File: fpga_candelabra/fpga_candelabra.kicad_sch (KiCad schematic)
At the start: 0 parts

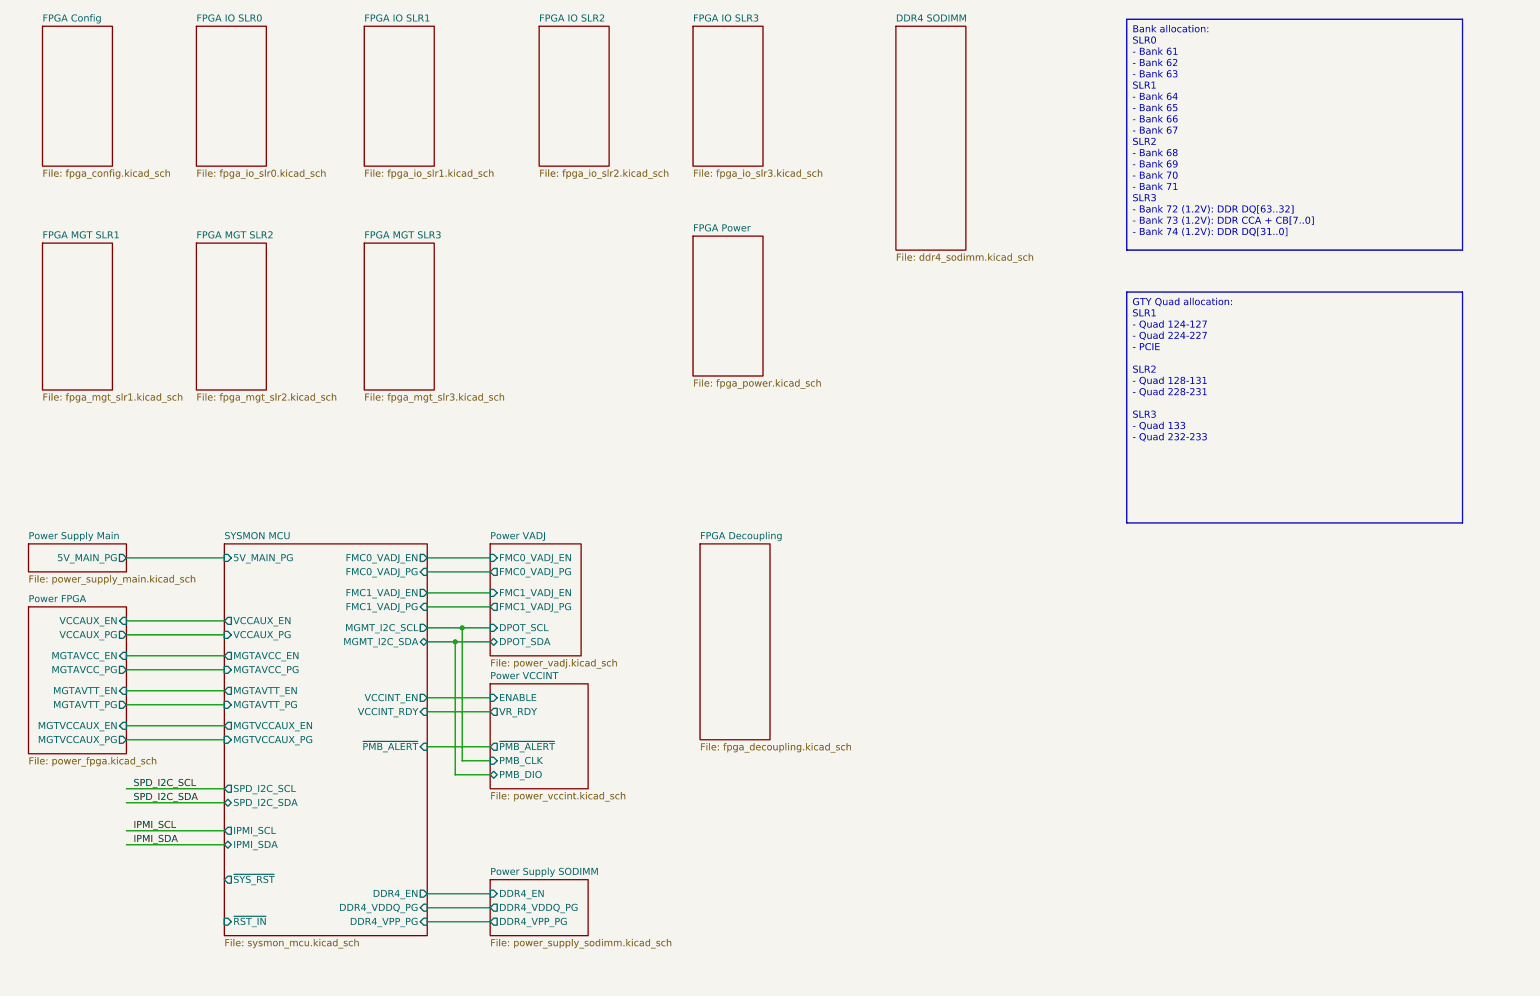
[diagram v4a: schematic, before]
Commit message: fpga_candelabra: use bus alias to connect ddr4
Signed-off-by: Yichuan Gao <gaoyichuan000@gmail.com>
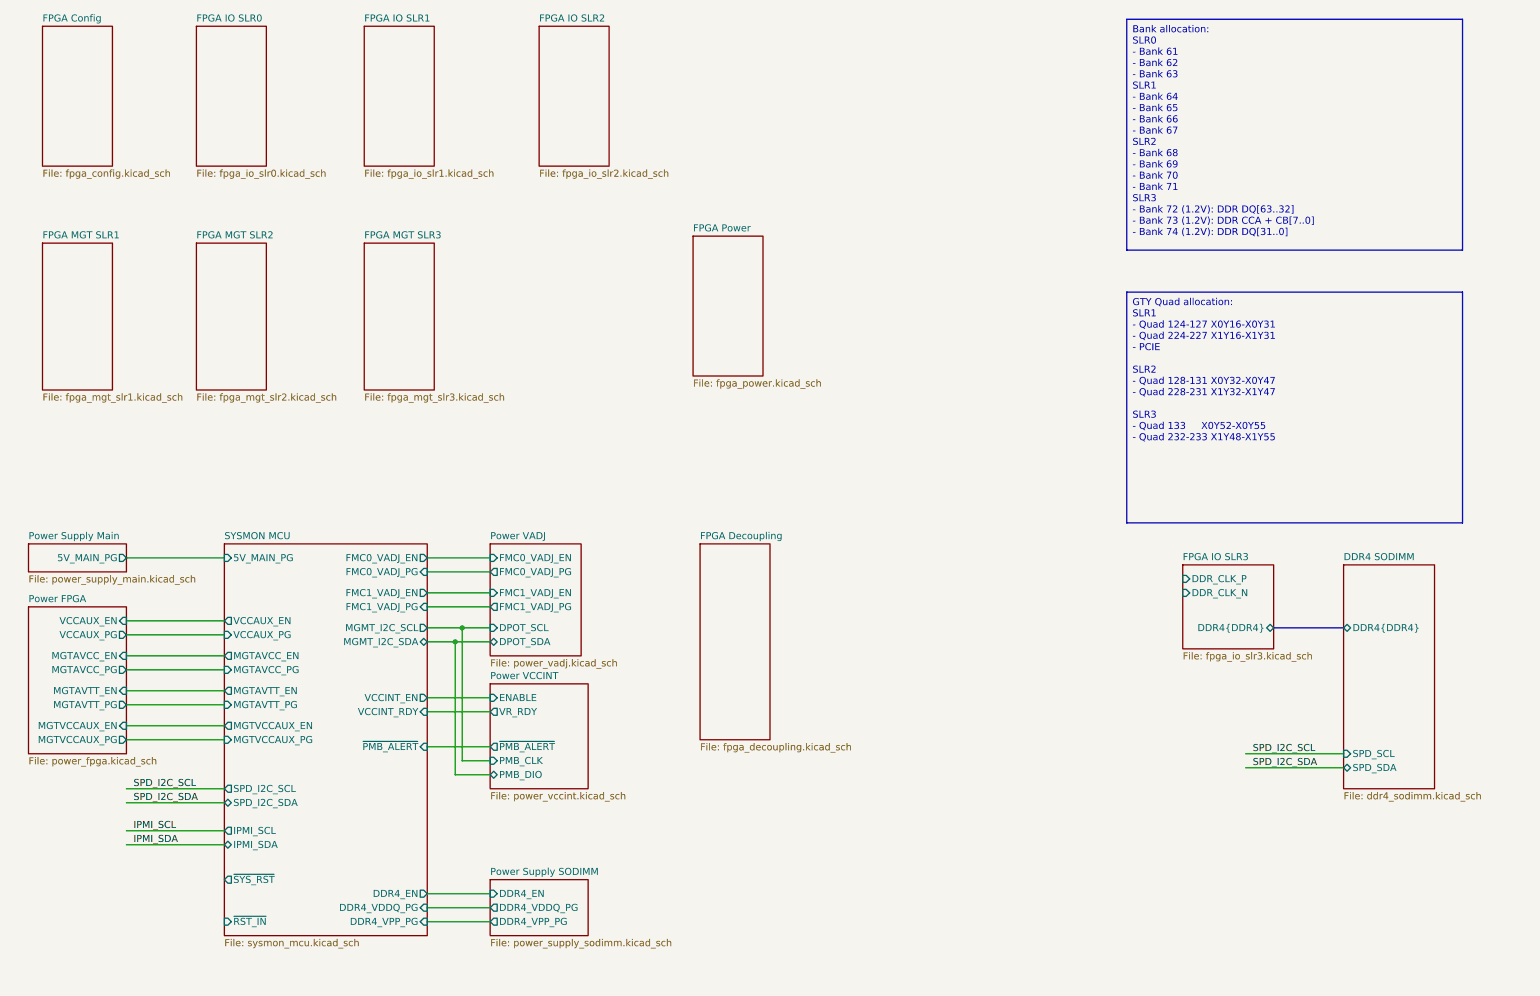
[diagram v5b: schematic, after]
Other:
- sheet DDR4 SODIMM ports: added DDR4{DDR4}, SPD_SCL, SPD_SDA; removed none
- sheet FPGA IO SLR3 ports: added DDR4{DDR4}, DDR_CLK_N, DDR_CLK_P; removed none
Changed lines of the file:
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@@
 	(generator_version "8.0")
 	(paper "A4")
+	(bus_alias "DDR4"
+		(members "A0" "A1" "A2" "A3" "A4" "A5" "A6" "A7" "A8" "A9" "A10" "A11"
+			"A12" "A13" "A14" "A15" "A16" "BA0" "BA1" "BG0" "BG1" "CK0+" "CK0-" "CKE0"
+			"CK1+" "CK1-" "CKE1" "CS0" "CS1" "CS2" "CS3" "ODT0" "ODT1" "~{ACT}" "PARITY"
+			"~{ALERT}" "~{RESET}" "DQS0+" "DQS1+" "DQS2+" "DQS3+" "DQS4+" "DQS5+"
+			"DQS6+" "DQS7+" "DQS8+" "DQS0-" "DQS1-" "DQS2-" "DQS3-" "DQS4-" "DQS5-"
+			"DQS6-" "DQS7-" "DQS8-" "DM0" "DM1" "DM2" "DM3" "DM4" "DM5" "DM6" "DM7"
+			"DM8" "DQ0" "DQ1" "DQ2" "DQ3" "DQ4" "DQ5" "DQ6" "DQ7" "DQ8" "DQ9" "DQ10"
+			"DQ11" "DQ12" "DQ13" "DQ14" "DQ15" "DQ16" "DQ17" "DQ18" "DQ19" "DQ20"
+			"DQ21" "DQ22" "DQ23" "DQ24" "DQ25" "DQ26" "DQ27" "DQ28" "DQ29" "DQ30"
+			"DQ31" "DQ32" "DQ33" "DQ34" "DQ35" "DQ36" "DQ37" "DQ38" "DQ39" "DQ40"
+			"DQ41" "DQ42" "DQ43" "DQ44" "DQ45" "DQ46" "DQ47" "DQ48" "DQ49" "DQ50"
+			"DQ51" "DQ52" "DQ53" "DQ54" "DQ55" "DQ56" "DQ57" "DQ58" "DQ59" "DQ60"
+			"DQ61" "DQ62" "DQ63" "CB0" "CB1" "CB2" "CB3" "CB4" "CB5" "CB6" "CB7"
+		)
+	)
 	(junction
 		(at 97.79 132.08)
@@
 		)
 	)
+	(bus
+		(pts
+			(xy 246.38 129.54) (xy 259.08 129.54)
+		)
+		(stroke
+			(width 0)
+			(type default)
+		)
+	)
 	(wire
 		(pts
@@
 	(wire
 		(pts
+			(xy 241.3 152.4) (xy 259.08 152.4)
+		)
+		(stroke
+			(width 0)
+			(type default)
+		)
+	)
+	(wire
+		(pts
 			(xy 38.1 128.27) (xy 55.88 128.27)
 		)
@@
 		(pts
 			(xy 99.06 153.67) (xy 104.14 153.67)
+		)
+		(stroke
+			(width 0)
+			(type default)
+		)
+	)
+	(wire
+		(pts
+			(xy 241.3 154.94) (xy 259.08 154.94)
 		)
 		(stroke
@@
 		)
 	)
-	(text_box "GTY Quad allocation:\nSLR1\n  - Quad 124-127\n  - Quad 224-227\n    - PCIE\n\nSLR2\n  - Quad 128-131\n  - Quad 228-231\n\nSLR3\n  - Quad 133\n  - Quad 232-233"
+	(text_box "GTY Quad allocation:\nSLR1\n  - Quad 124-127 X0Y16-X0Y31\n  - Quad 224-227 X1Y16-X1Y31\n    - PCIE\n\nSLR2\n  - Quad 128-131 X0Y32-X0Y47\n  - Quad 228-231 X1Y32-X1Y47\n\nSLR3\n  - Quad 133     X0Y52-X0Y55\n  - Quad 232-233 X1Y48-X1Y55"
 		(exclude_from_sim no)
 		(at 219.71 68.58 0)
@@
 		)
 	)
+	(label "SPD_I2C_SDA"
+		(at 242.57 154.94 0)
+		(fields_autoplaced yes)
+		(effects
+			(font
+				(size 1.27 1.27)
+			)
+			(justify left bottom)
+		)
+	)
 	(label "IPMI_SDA"
 		(at 39.37 168.91 0)
+		(fields_autoplaced yes)
+		(effects
+			(font
+				(size 1.27 1.27)
+			)
+			(justify left bottom)
+		)
+	)
+	(label "SPD_I2C_SCL"
+		(at 242.57 152.4 0)
 		(fields_autoplaced yes)
 		(effects
@@
 	)
 	(sheet
-		(at 140.97 20.32)
-		(size 12.7 25.4)
+		(at 229.87 118.11)
+		(size 16.51 15.24)
 		(fields_autoplaced yes)
 		(stroke
@@
 		)
 		(property "Sheetname" "FPGA IO SLR3"
-			(at 140.97 19.6084 0)
+			(at 229.87 117.3984 0)
 			(effects
 				(font
@@
 		)
 		(property "Sheetfile" "fpga_io_slr3.kicad_sch"
-			(at 140.97 46.3046 0)
+			(at 229.87 133.9346 0)
 			(effects
 				(font
@@
 				)
 				(justify left top)
+			)
+		)
+		(pin "DDR_CLK_N" input
+			(at 229.87 123.19 180)
+			(effects
+				(font
+					(size 1.27 1.27)
+				)
+				(justify left)
+			)
+		)
+		(pin "DDR_CLK_P" input
+			(at 229.87 120.65 180)
+			(effects
+				(font
+					(size 1.27 1.27)
+				)
+				(justify left)
+			)
+		)
+		(pin "DDR4{DDR4}" bidirectional
+			(at 246.38 129.54 0)
+			(effects
+				(font
+					(size 1.27 1.27)
+				)
+				(justify right)
 			)
 		)
@@
 	)
 	(sheet
-		(at 177.8 20.32)
-		(size 12.7 40.64)
+		(at 259.08 118.11)
+		(size 16.51 40.64)
 		(fields_autoplaced yes)
 		(stroke
@@
 		)
 		(property "Sheetname" "DDR4 SODIMM"
-			(at 177.8 19.6084 0)
+			(at 259.08 117.3984 0)
 			(effects
 				(font
@@
 		)
 		(property "Sheetfile" "ddr4_sodimm.kicad_sch"
-			(at 177.8 61.5446 0)
+			(at 259.08 159.3346 0)
 			(effects
 				(font
@@
 			)
 		)
+		(pin "SPD_SCL" input
+			(at 259.08 152.4 180)
+			(effects
+				(font
+					(size 1.27 1.27)
+				)
+				(justify left)
+			)
+		)
+		(pin "SPD_SDA" bidirectional
+			(at 259.08 154.94 180)
+			(effects
+				(font
+					(size 1.27 1.27)
+				)
+				(justify left)
+			)
+		)
+		(pin "DDR4{DDR4}" bidirectional
+			(at 259.08 129.54 180)
+			(effects
+				(font
+					(size 1.27 1.27)
+				)
+				(justify left)
+			)
+		)

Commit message: fpga_candelabra: add clock pll, refactor fmc power
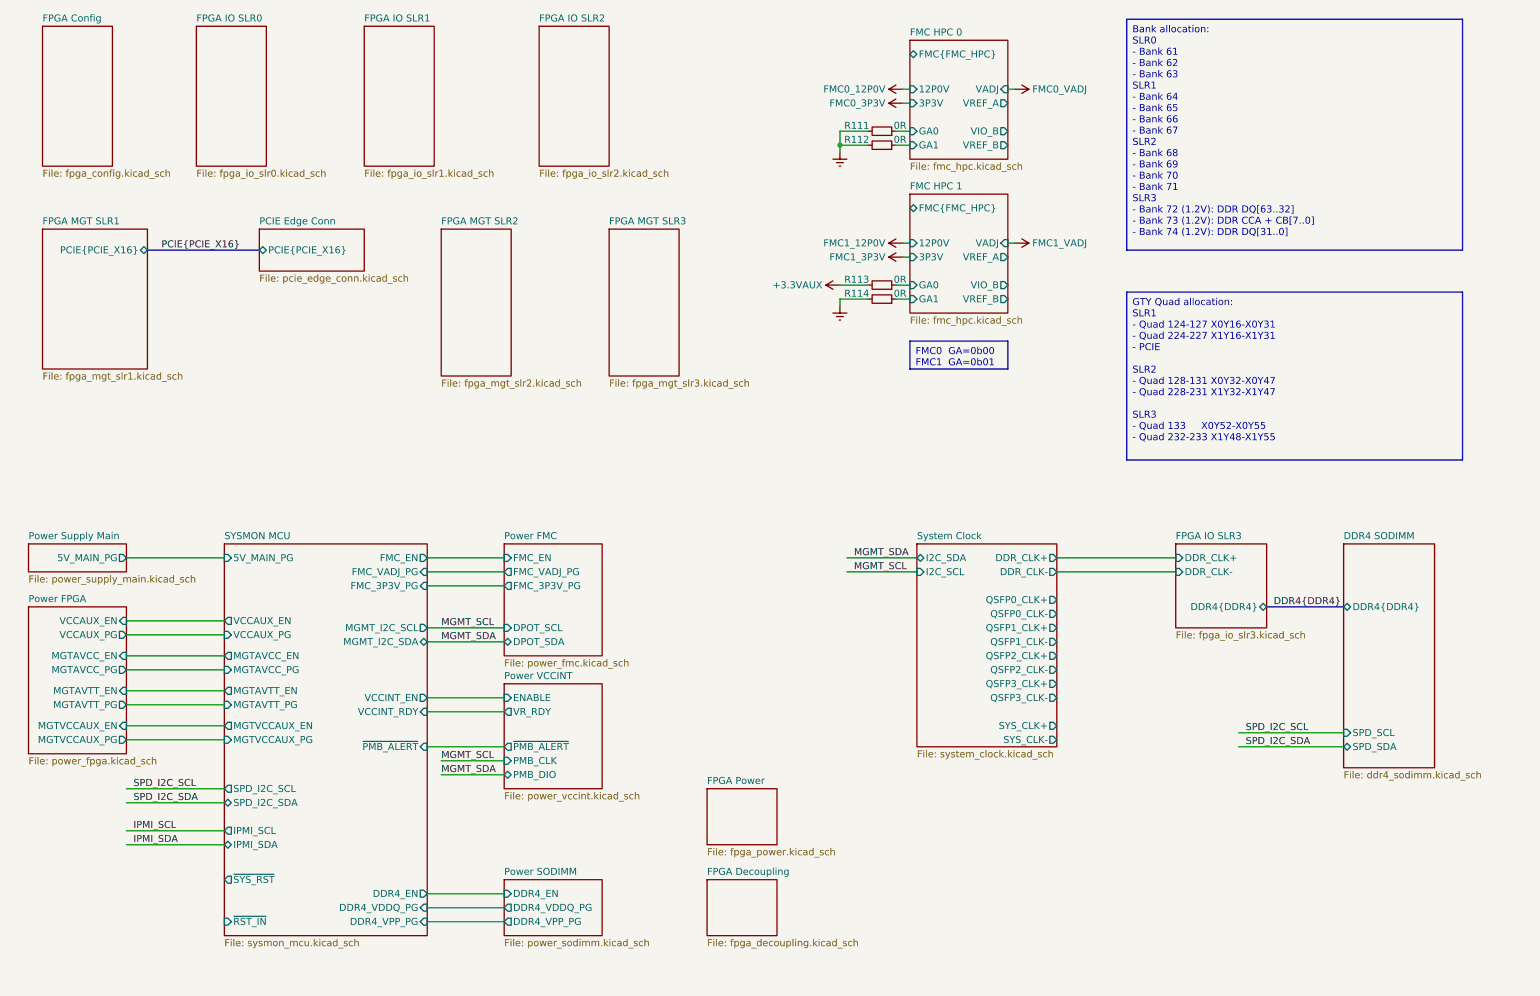
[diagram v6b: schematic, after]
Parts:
- added R111, R112, R113, R114: 0R, Resistor_SMD:R_0402_1005Metric, symbol Device:R_Small
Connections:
- new net +3.3VAUX: R113.2
- new net Earth: R111.2, R112.2, R114.2
- new net FMC HPC 0/GA0: R111.1
- new net FMC HPC 0/GA1: R112.1
- new net FMC HPC 1/GA0: R113.1
- new net FMC HPC 1/GA1: R114.1
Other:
- sheet Power Supply SODIMM renamed Power SODIMM
- sheet Power VADJ renamed Power FMC
- added sheet FMC HPC 0 (fmc_hpc.kicad_sch)
- added sheet FMC HPC 1 (fmc_hpc.kicad_sch)
- added sheet PCIE Edge Conn (pcie_edge_conn.kicad_sch)
- added sheet System Clock (system_clock.kicad_sch)
- sheet FPGA IO SLR3 ports: added DDR_CLK+, DDR_CLK-; removed DDR_CLK_N, DDR_CLK_P
- sheet FPGA MGT SLR1 ports: added PCIE{PCIE_X16}; removed none
- sheet Power FMC: file power_vadj.kicad_sch -> power_fmc.kicad_sch
- sheet Power FMC ports: added FMC_3P3V_PG, FMC_EN, FMC_VADJ_PG; removed FMC0_VADJ_EN, FMC0_VADJ_PG, FMC1_VADJ_EN, FMC1_VADJ_PG
- sheet Power SODIMM: file power_supply_sodimm.kicad_sch -> power_sodimm.kicad_sch
- sheet SYSMON MCU ports: added FMC_3P3V_PG, FMC_EN, FMC_VADJ_PG; removed FMC0_VADJ_EN, FMC0_VADJ_PG, FMC1_VADJ_EN, FMC1_VADJ_PG

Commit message: candelabra: add i-pex extension ports, remove FMC1
* update bank/mgt allocation
* add basic pcb floorplanning

Signed-off-by: Yichuan Gao <gaoyichuan000@gmail.com>
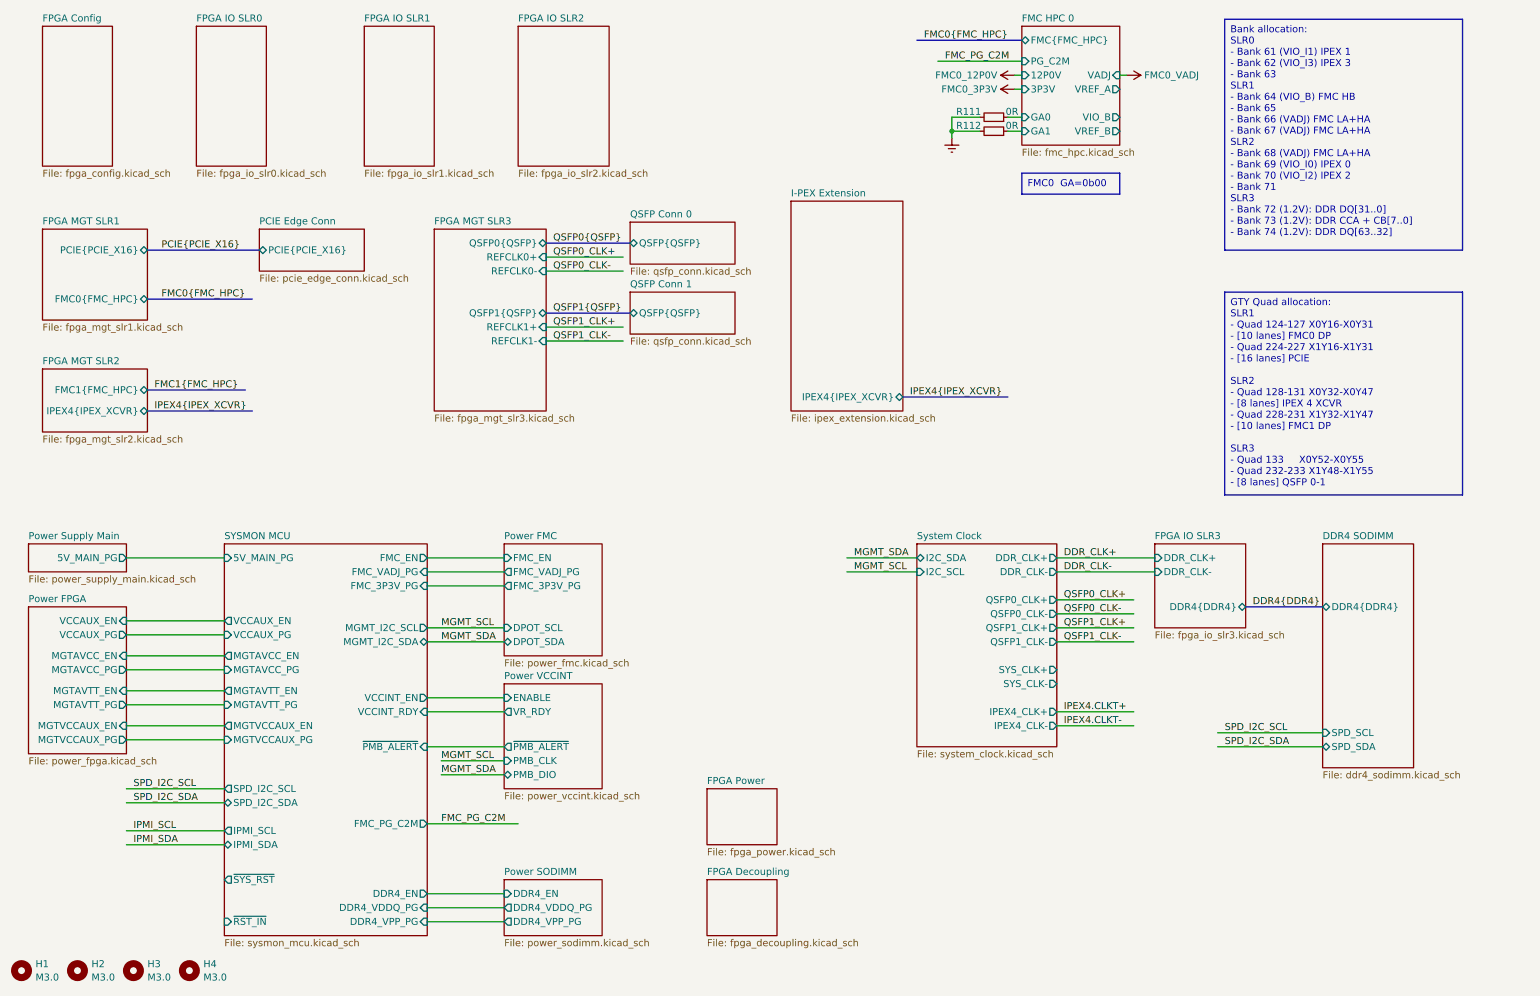
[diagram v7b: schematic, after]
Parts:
- removed R113, R114: 0R, Resistor_SMD:R_0402_1005Metric, symbol Device:R_Small
- added H1, H2, H3, H4: M3.0, MountingHole:MountingHole_3.2mm_M3_DIN965, symbol CHIPSAlliance_Mechanical:MountingHole
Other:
- removed sheet FMC HPC 1
- added sheet I-PEX Extension (ipex_extension.kicad_sch)
- added sheet QSFP Conn 0 (qsfp_conn.kicad_sch)
- added sheet QSFP Conn 1 (qsfp_conn.kicad_sch)
- sheet FMC HPC 0 ports: added PG_C2M; removed none
- sheet FPGA MGT SLR1 ports: added FMC0{FMC_HPC}; removed none
- sheet FPGA MGT SLR2 ports: added FMC1{FMC_HPC}, IPEX4{IPEX_XCVR}; removed none
- sheet FPGA MGT SLR3 ports: added QSFP0{QSFP}, QSFP1{QSFP}, REFCLK0+, REFCLK0-, REFCLK1+, REFCLK1-; removed none
- sheet SYSMON MCU ports: added FMC_PG_C2M; removed none
- sheet System Clock ports: added IPEX4_CLK+, IPEX4_CLK-; removed QSFP2_CLK+, QSFP2_CLK-, QSFP3_CLK+, QSFP3_CLK-
- moved on the sheet: R111, R112
